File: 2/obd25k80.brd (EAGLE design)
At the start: 96.5 x 50.8 mm, 56 parts, among them IC1 PIC18F25K80, IC2 MCP2562, IC3 78L05, IC4 78L05, IC5 LE33CZ, J1 MA04-1, J2 DB9-M, Q1 BC547, Q2 BC557, Q3 BC547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

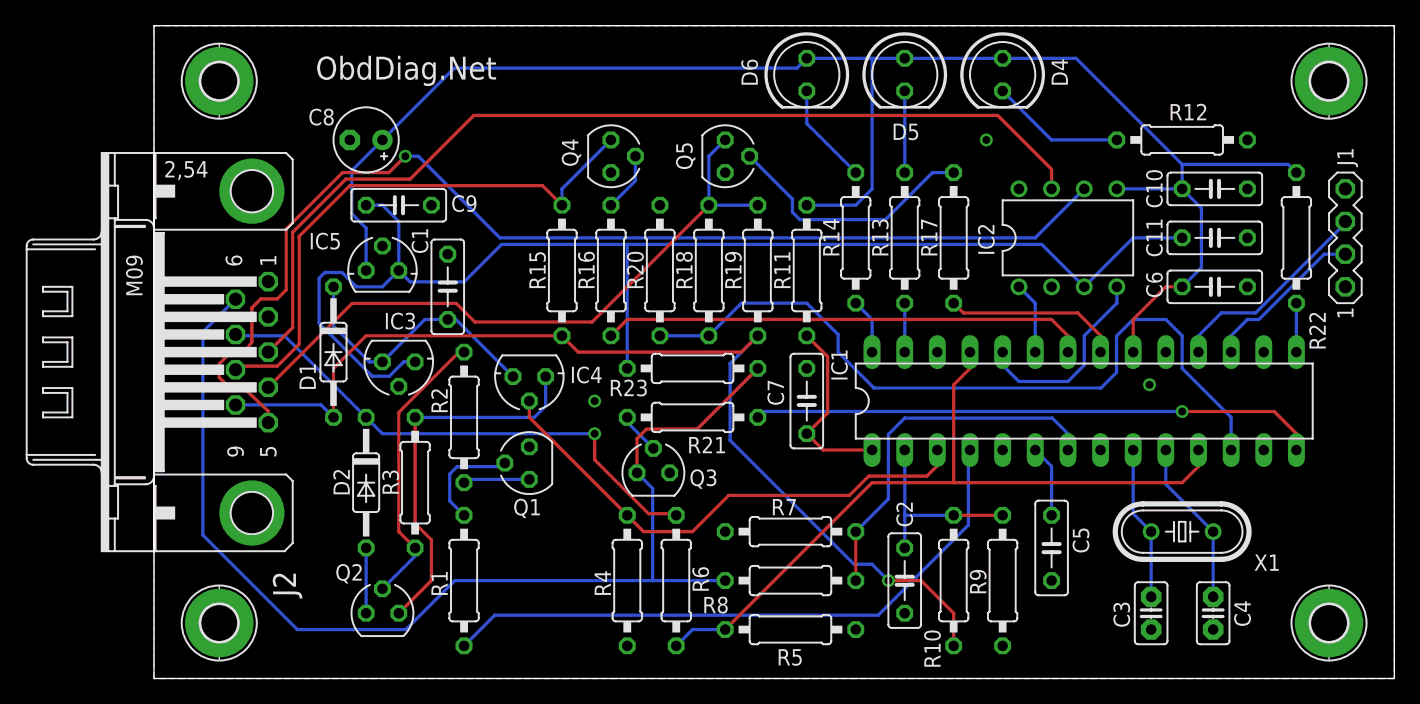
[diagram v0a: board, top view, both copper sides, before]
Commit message: Reimplemented with ULN2003
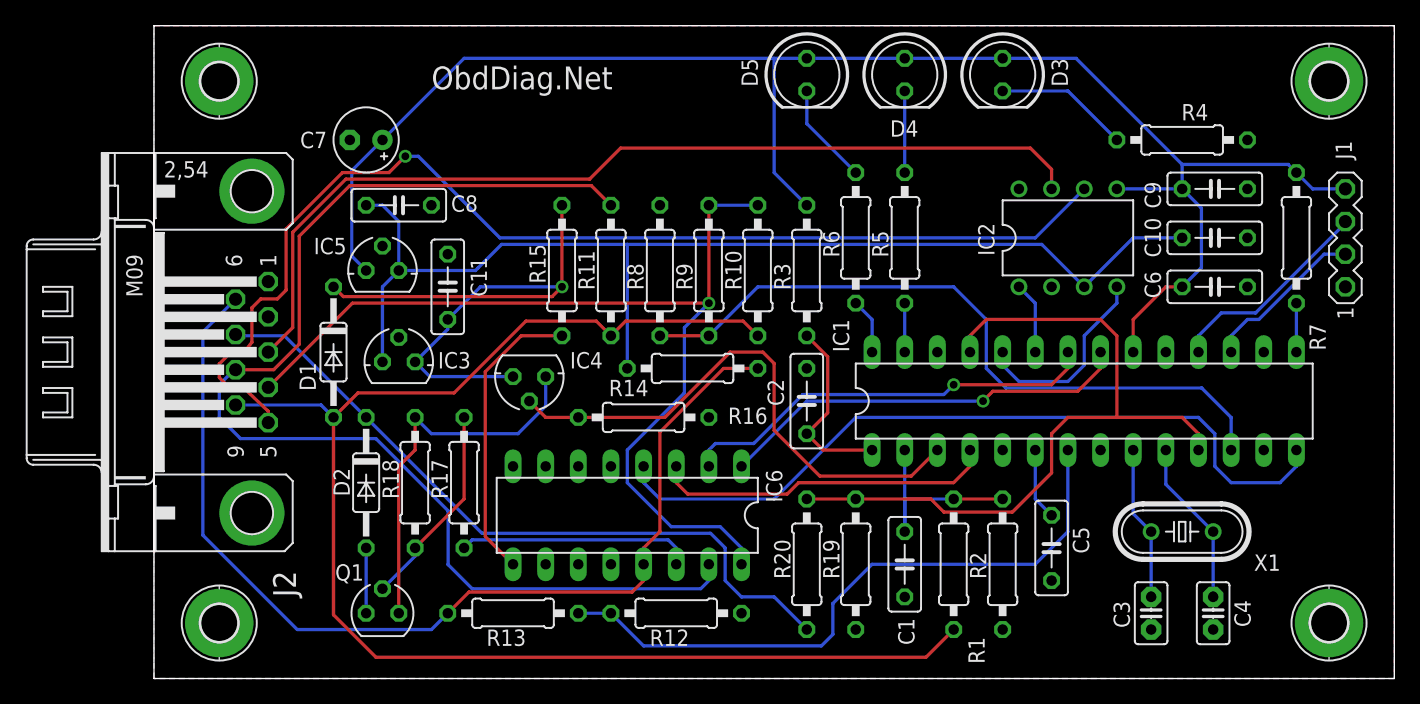
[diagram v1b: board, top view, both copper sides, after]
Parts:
- removed D6: (no value), led:LED5MM
- removed Q2: BC557, transistor-small-signal:SOT54A
- removed Q3, Q4, Q5: BC547, transistor-small-signal:SOT54A
- removed R21: 4.7K, rcl:0207/10
- removed R22: 10K, rcl:0207/10
- removed R23: 22K, rcl:0207/10
- added D3: (no value), led:LED5MM
- added IC6: ULN2003AN, uln-udn:DIL16
- C7: value 100nF -> 1.5uF; device rcl:C050-025X075 -> rcl:E2,5-5
- C8: value 1.5uF -> 100nF; device rcl:E2,5-5 -> rcl:C050-025X075
- Q1: value BC547 -> BC557
- R1: value 4.7K -> 47K
- R10: value 47K -> 510
- R11: value 10K -> 510
- R12: value 330 -> 15K
- R13, R14: value 330 -> 22K
- R15: value 510 -> 10K
- R16: value 2.2K -> 10K
- R17: value 2.2K -> 4.7K
- R18: value 47K -> 10K
- R19: value 510 -> 15K
- R2: value 4.7K -> 10K
- R4: value 10K -> 330
- R5: value 15K -> 330
- R6: value 22K -> 330
- R7: value 15K -> 10K
- R9: value 10K -> 47K
- moved C9 63.5 mm to (82.5, 38.1)
- moved C11 59.8 mm to (22.9, 30.5), turned to 90 degrees
- moved R4 55.1 mm to (80.0, 41.9), turned to 180 degrees
- moved R12 53.9 mm to (40.6, 5.08)
- moved R7 45.5 mm to (88.9, 34.3), turned to 90 degrees
- moved R2 43.4 mm to (66.0, 8.89), turned to 270 degrees
- moved R17 42.6 mm to (24.1, 15.2)
- moved R13 42.2 mm to (27.9, 5.08), turned to 0 degrees
- moved C1 41.6 mm to (58.4, 8.89), turned to 270 degrees
- moved C7 39.9 mm to (16.5, 41.9), turned to 180 degrees
- moved R1 38.1 mm to (62.2, 8.89)
- moved R3 34.7 mm to (50.8, 31.8), turned to 270 degrees
- moved R9 33.2 mm to (43.2, 31.8), turned to 90 degrees
- moved R5 31.8 mm to (58.4, 34.3), turned to 90 degrees
- moved R6 30.1 mm to (54.6, 34.3), turned to 90 degrees
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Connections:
- removed net N$15: Q4.B, R16.2
- removed net N$20: IC1.21, R17.1
- removed net N$22: Q3.B, R21.2
- removed net N$24: Q5.B, R17.2
- removed net N$28: Q1.B, R1.2
- removed net N$9: IC1.22, R16.1
- new net N$4: IC6.9, R15.1
- new net RB0: IC1.21, IC6.1
- new net RB1: IC1.22, IC6.2
- net +12V: now also C11.1, R15.2; no longer C1.1
- net +3V3: now also C7.+, C9.1, D3.A, J1.4, R3.1, R7.2; no longer C10.1, C8.+, D6.A, R11.1, R22.2
- net +5V: now also C10.1, C8.1, R14.2; no longer C11.1, C9.1, R23.2
- net C2INB: now also R12.2, R13.2; no longer R7.2, R8.2
- net GND: now also C7.-, C8.2, IC6.8, R16.1, R19.1, R2.2, R8.2; no longer C7.2, C8.-, Q1.E, Q3.E, Q4.E, Q5.E, R20.2, R5.1, R7.1, R9.2
- net ISO-K: now also IC6.16, R10.1, R9.2; no longer Q5.C, R18.2, R19.1
- net ISO-L: now also IC6.15, R11.1; no longer Q4.C, R15.1
- net J+DIV: now also R19.2, R20.2; no longer R5.2, R6.2
- net J1850+: now also R20.1; no longer R6.1
- net J1850-: now also IC6.13, R13.1, R14.1; no longer Q3.C, R23.1, R8.1
- net N$1: now also D3.K, R4.2; no longer D4.K, R12.2
- net N$10: now also D5.K, R6.2; no longer D6.K, R14.2
- net N$11: now also R5.1; no longer R13.1
- net N$2: now also R6.1; no longer R14.1
- net N$25: now also IC6.14, R17.1; no longer Q1.C, R2.1
- net N$26: now also C1.1, R1.2, R2.1; no longer C2.1, R10.2, R9.1
- net N$3: now also R7.1; no longer R22.1
- net N$30: now also Q1.B, R17.2, R18.1; no longer Q2.B, R2.2, R3.1
- net N$31: now also Q1.E, R18.2; no longer Q2.E, R3.2
- net N$32: now also Q1.C; no longer Q2.C
- net N$6: now also D4.K, R5.2; no longer D5.K, R13.2
- net N$7: now also C2.1, R3.2; no longer C7.1, R11.2
- net RA1: now also R16.2; no longer R4.2
- net RA2: now also IC6.3; no longer R1.1
- net RC1: now also R8.1, R9.1; no longer R18.1, R20.1
- net RC3: now also IC6.4; no longer R21.1
- net V+: now also R1.1, R10.2, R11.2; no longer R10.1, R15.2, R19.2
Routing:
- net ISO-L: track 43.5 -> 92.6 mm
- net N$9: track 37.9 -> 0.00 mm
- net RB1: track 0.00 -> 33.1 mm, vias 0 -> 1
- net RB0: track 0.00 -> 32.4 mm, vias 0 -> 1
- net V+: track 81.5 -> 111.5 mm, vias 1 -> 0
- net ISO-K: track 50.8 -> 77.3 mm, vias 0 -> 1
- net +12V: track 21.4 -> 47.2 mm, vias 0 -> 1
- net N$4: track 0.00 -> 23.0 mm
- net RA2: track 49.0 -> 26.7 mm
- net C2INB: track 28.9 -> 50.6 mm
- net N$24: track 20.0 -> 0.00 mm
- net RC3: track 44.1 -> 60.6 mm, vias 1 -> 0
- net J1850+: track 41.3 -> 55.4 mm, vias 1 -> 0
- net N$20: track 13.8 -> 0.00 mm
- net +5V: track 102.5 -> 88.9 mm
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
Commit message: A few optimizations
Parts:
- moved R14 5.39 mm to (38.1, 20.3), turned to 0 degrees
- moved R16 4.58 mm to (40.6, 24.1)
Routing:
- net J1850-: track 80.1 -> 69.4 mm
- net ISO-K: track 77.3 -> 71.5 mm
- net +5V: track 88.9 -> 93.4 mm
- net RA2: track 26.7 -> 28.7 mm
- net RB0: track 32.4 -> 34.3 mm, vias 1 -> 0
- net CAN-L: track 89.4 -> 90.6 mm
- net RA1: track 42.3 -> 43.3 mm
- net RB1: track 33.1 -> 33.9 mm, vias 1 -> 0

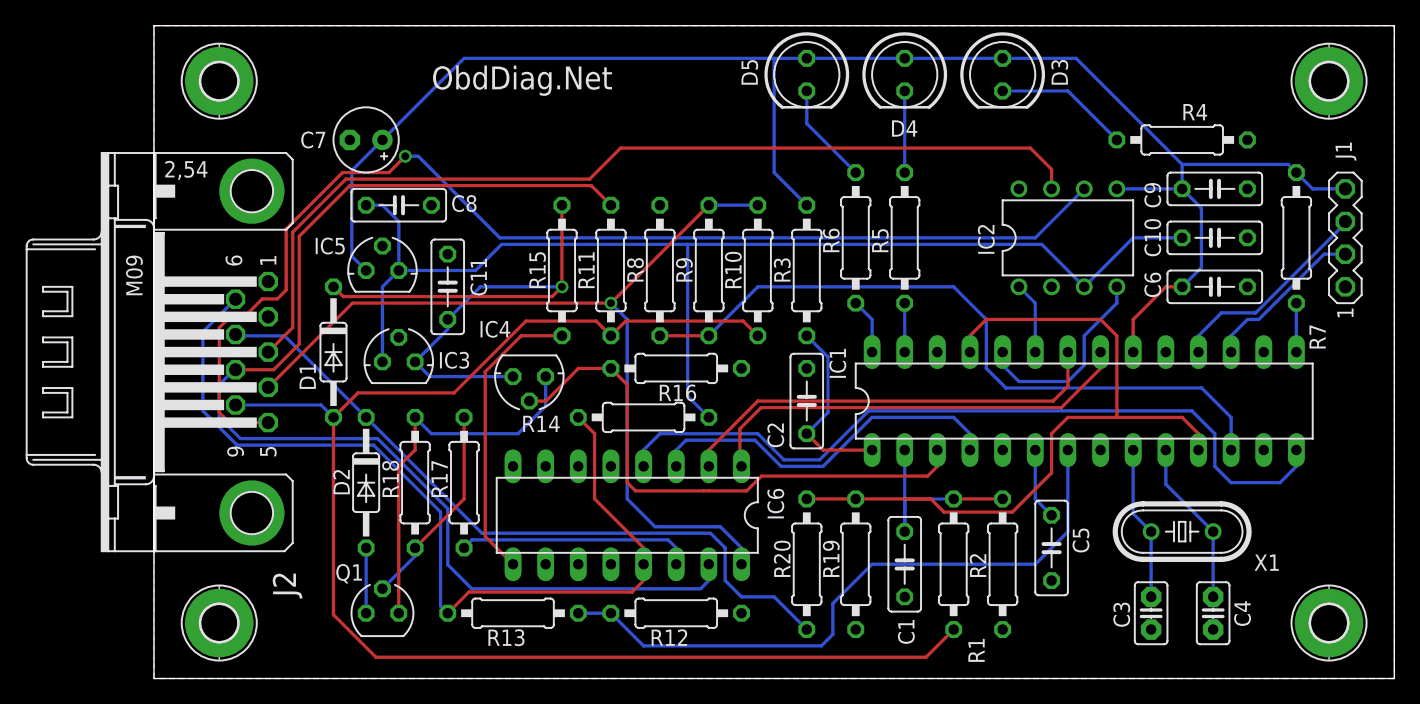
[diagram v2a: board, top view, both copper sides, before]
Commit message: Another 3.3V LDO
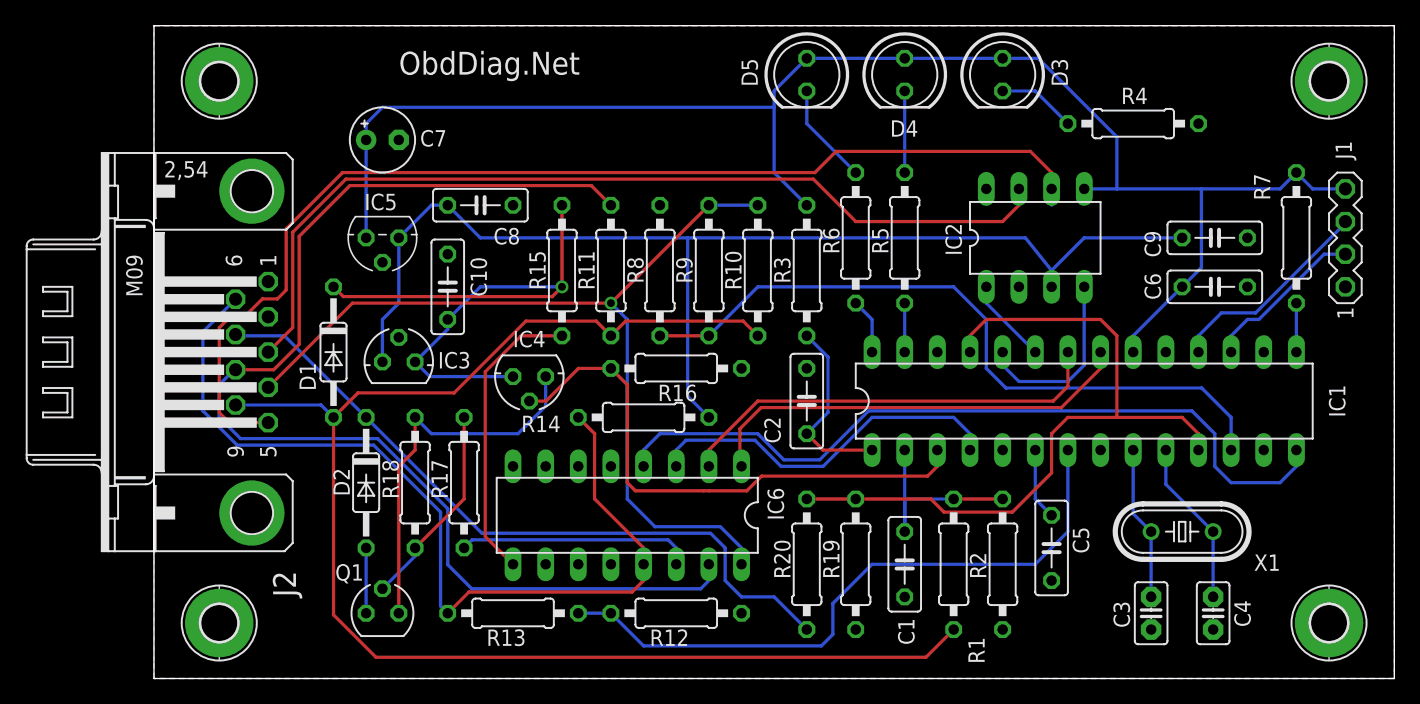
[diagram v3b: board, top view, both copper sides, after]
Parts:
- removed C11: 100nF, rcl:C050-025X075
- C7: value 1.5uF -> 2.2uF
- IC2: value MCP2562 -> MCP25621
- IC5: value LE33CZ -> AP7384-3.3; device v-reg:78LXX -> obddiag-net:TO92
- R2: value 10K -> 6.2K
- R8: value 22K -> 18K
- moved C10 59.8 mm to (22.9, 30.5), turned to 90 degrees
- moved C8 6.35 mm to (25.4, 36.8)
- moved R4 4.02 mm to (76.2, 43.2)
- moved C9 3.81 mm to (82.5, 34.3)
- moved IC2 2.54 mm to (68.6, 34.3)
- moved IC5 2.54 mm to (17.8, 34.3), turned to 180 degrees
- moved C7 1.27 mm to (17.8, 41.9), turned to 0 degrees
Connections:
- net +12V: now also C10.1; no longer C11.1
- net +3V3: now also IC5.3; no longer C9.1, IC5.OUT
- net +5V: now also C9.1, IC5.1; no longer C10.1, IC5.IN
- net GND: now also IC5.2; no longer C11.2, IC5.GND
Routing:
- net +3V3: track 129.1 -> 121.7 mm
- net N$1: track 10.5 -> 6.13 mm
- net CAN-L: track 90.6 -> 87.2 mm, vias 1 -> 0
- net CAN-H: track 74.1 -> 71.5 mm
- net +5V: track 93.4 -> 91.4 mm
- net J1850-: track 69.4 -> 70.7 mm
- net N$17: track 15.6 -> 14.5 mm
- net N$23: track 5.61 -> 6.66 mm
